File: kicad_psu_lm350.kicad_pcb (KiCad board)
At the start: 2 copper layers, 149.9 x 83.8 mm, 28 parts, among them J1 AC Input, J2 AC Input, J3 DC +1.25 to +30V, J4 GND, J5 GND, J6 GND, J7 GND, U1 LM350_TO220

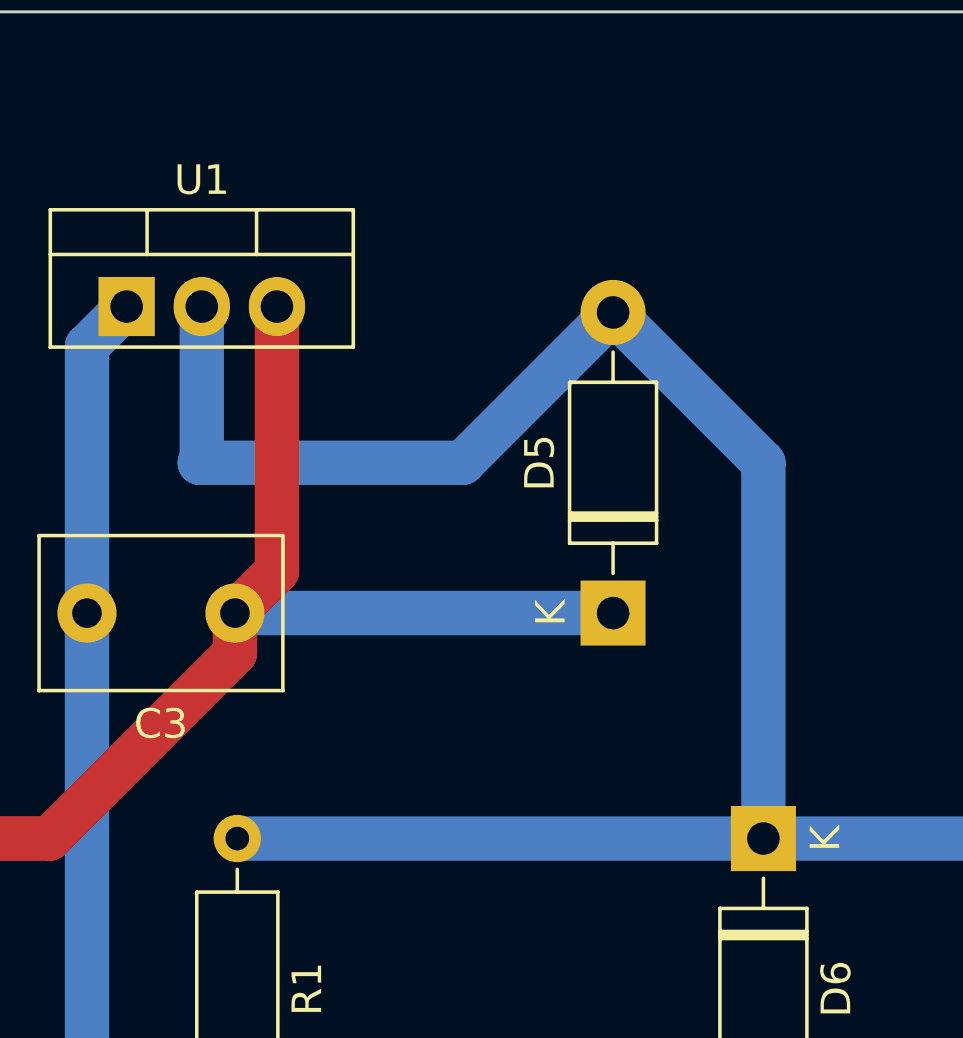
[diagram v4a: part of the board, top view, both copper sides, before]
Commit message: Created prototype - manufactured on pcbway.com
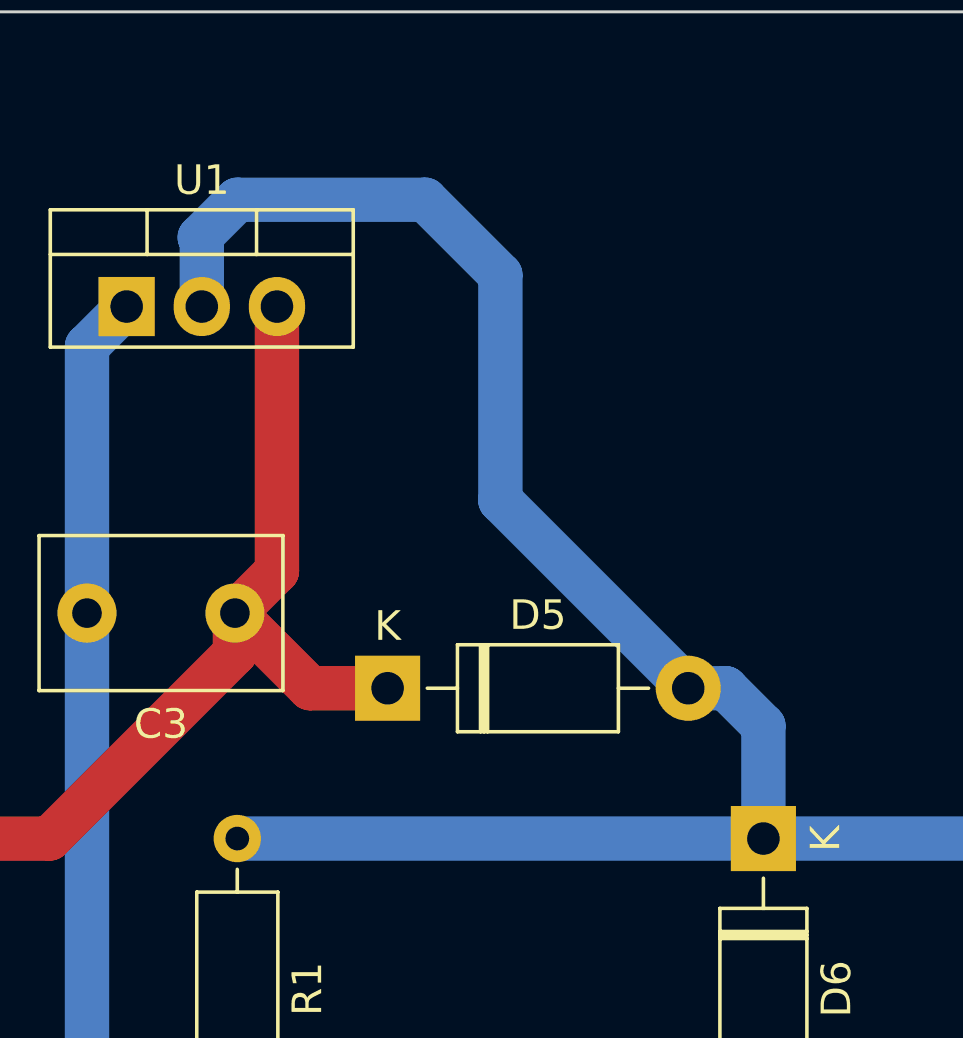
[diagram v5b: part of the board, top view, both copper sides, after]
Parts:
- moved D5 8.03 mm to (215.9, 50.8), turned to 0 degrees
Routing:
- net Net-(C1-Pad1): track 137.4 -> 130.8 mm
- net Net-(C5-Pad1): track 114.6 -> 110.9 mm
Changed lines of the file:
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@@
       (disableapertmacros false)
       (usegerberextensions false)
-      (usegerberattributes true)
-      (usegerberadvancedattributes true)
-      (creategerberjobfile true)
+      (usegerberattributes false)
+      (usegerberadvancedattributes false)
+      (creategerberjobfile false)
       (dashed_line_dash_ratio 12.000000)
       (dashed_line_gap_ratio 3.000000)
@@
       (psa4output false)
       (plotreference true)
-      (plotvalue true)
+      (plotvalue false)
       (plotinvisibletext false)
       (sketchpadsonfab false)
-      (subtractmaskfromsilk false)
+      (subtractmaskfromsilk true)
       (outputformat 1)
       (mirror false)
-      (drillshape 1)
+      (drillshape 0)
       (scaleselection 1)
-      (outputdirectory "")
+      (outputdirectory "outputs/pcbway/")
     )
   )
@@
   )
   (footprint "Diode_THT:D_DO-41_SOD81_P10.16mm_Horizontal" (layer "F.Cu")
-    (at 223.52 48.26 90)
+    (at 215.9 50.8)
     (descr "Diode, DO-41_SOD81 series, Axial, Horizontal, pin pitch=10.16mm, , length*diameter=5.2*2.7mm^2, , http://www.diodes.com/_files/packages/DO-41%20(Plastic).pdf")
     (tags "Diode DO-41_SOD81 series Axial Horizontal pin pitch 10.16mm  length 5.2mm diameter 2.7mm")
@@
     (property "Sheetname" "")
     (attr through_hole)
-    (fp_text reference "D5" (at 5.08 -2.47 90) (layer "F.SilkS")
+    (fp_text reference "D5" (at 5.08 -2.47) (layer "F.SilkS")
         (effects (font (size 1 1) (thickness 0.15)))
     )
-    (fp_text value "1N4007" (at 5.08 2.47 90) (layer "F.Fab")
+    (fp_text value "1N4007" (at 5.08 2.47) (layer "F.Fab")
         (effects (font (size 1 1) (thickness 0.15)))
     )
-    (fp_text user "K" (at 0 -2.1 90) (layer "F.SilkS")
+    (fp_text user "K" (at 0 -2.1) (layer "F.SilkS")
         (effects (font (size 1 1) (thickness 0.15)))
     )
-    (fp_text user "K" (at 0 -2.1 90) (layer "F.Fab")
+    (fp_text user "K" (at 0 -2.1) (layer "F.Fab")
         (effects (font (size 1 1) (thickness 0.15)))
     )
-    (fp_text user "${REFERENCE}" (at 5.47 0 90) (layer "F.Fab")
+    (fp_text user "${REFERENCE}" (at 5.47 0) (layer "F.Fab")
         (effects (font (size 1 1) (thickness 0.15)))
     )
@@
     (fp_line (start 10.16 0) (end 7.68 0)
       (stroke (width 0.1) (type solid)) (layer "F.Fab"))
-    (pad "1" thru_hole rect (at 0 0 90) (size 2.2 2.2) (drill 1.1) (layers "*.Cu" "*.Mask")
+    (pad "1" thru_hole rect (at 0 0) (size 2.2 2.2) (drill 1.1) (layers "*.Cu" "*.Mask")
       (net 4 "Net-(C1-Pad1)") (pinfunction "K") (pintype "passive"))
-    (pad "2" thru_hole oval (at 10.16 0 90) (size 2.2 2.2) (drill 1.1) (layers "*.Cu" "*.Mask")
+    (pad "2" thru_hole oval (at 10.16 0) (size 2.2 2.2) (drill 1.1) (layers "*.Cu" "*.Mask")
       (net 1 "Net-(C5-Pad1)") (pinfunction "A") (pintype "passive"))
     (model "${KICAD6_3DMODEL_DIR}/Diode_THT.3dshapes/D_DO-41_SOD81_P10.16mm_Horizontal.wrl"
@@
     (pts (xy 116.84 111.76) (xy 266.7 111.76))
     (height 5.08)
-    (gr_text "149.8600 mm" (at 191.77 115.69) (layer "Dwgs.User")
+    (gr_text "5.9000 in" (at 191.77 115.69) (layer "Dwgs.User")
       (effects (font (size 1 1) (thickness 0.15)))
     )
@@
     (pts (xy 116.84 27.94) (xy 116.84 111.76))
     (height 7.62)
-    (gr_text "83.8200 mm" (at 108.07 69.85 90) (layer "Dwgs.User")
+    (gr_text "3.3000 in" (at 108.07 69.85 90) (layer "Dwgs.User")
       (effects (font (size 1 1) (thickness 0.15)))
     )
@@
   (via (at 259.08 35.56) (size 5) (drill 3) (layers "F.Cu" "B.Cu") (net 0))
   (via (at 124.46 104.14) (size 5) (drill 3) (layers "F.Cu" "B.Cu") (net 0))
-  (segment (start 209.62 43.11) (end 209.62 37.9) (width 1.5) (layer "B.Cu") (net 1))
   (segment (start 242.26 82.86) (end 247.65 77.47) (width 1.5) (layer "B.Cu") (net 1))
+  (segment (start 219.71 44.45) (end 219.71 36.83) (width 1.5) (layer "B.Cu") (net 1))
+  (segment (start 210.82 34.29) (end 209.55 35.56) (width 1.5) (layer "B.Cu") (net 1))
   (segment (start 241.3 55.88) (end 247.65 55.88) (width 1.5) (layer "B.Cu") (net 1))
-  (segment (start 209.55 43.18) (end 209.62 43.11) (width 1.5) (layer "B.Cu") (net 1))
   (segment (start 242.26 83.82) (end 242.26 82.86) (width 1.5) (layer "B.Cu") (net 1))
+  (segment (start 217.17 34.29) (end 210.82 34.29) (width 1.5) (layer "B.Cu") (net 1))
   (segment (start 247.65 55.88) (end 254 55.88) (width 1.5) (layer "B.Cu") (net 1))
   (segment (start 228.6 55.88) (end 241.3 55.88) (width 1.5) (layer "B.Cu") (net 1))
-  (segment (start 223.52 38.1) (end 218.44 43.18) (width 1.5) (layer "B.Cu") (net 1))
-  (segment (start 228.6 55.88) (end 228.6 43.18) (width 1.5) (layer "B.Cu") (net 1))
+  (segment (start 226.06 50.8) (end 227.33 50.8) (width 1.5) (layer "B.Cu") (net 1))
+  (segment (start 219.71 36.83) (end 217.17 34.29) (width 1.5) (layer "B.Cu") (net 1))
+  (segment (start 227.33 50.8) (end 228.6 52.07) (width 1.5) (layer "B.Cu") (net 1))
   (segment (start 247.65 77.47) (end 247.65 55.88) (width 1.5) (layer "B.Cu") (net 1))
   (segment (start 210.82 55.88) (end 228.6 55.88) (width 1.5) (layer "B.Cu") (net 1))
-  (segment (start 218.44 43.18) (end 209.55 43.18) (width 1.5) (layer "B.Cu") (net 1))
-  (segment (start 228.6 43.18) (end 223.52 38.1) (width 1.5) (layer "B.Cu") (net 1))
+  (segment (start 209.55 35.56) (end 209.62 35.63) (width 1.5) (layer "B.Cu") (net 1))
+  (segment (start 226.06 50.8) (end 219.71 44.45) (width 1.5) (layer "B.Cu") (net 1))
+  (segment (start 228.6 52.07) (end 228.6 55.88) (width 1.5) (layer "B.Cu") (net 1))
+  (segment (start 209.62 35.63) (end 209.62 37.9) (width 1.5) (layer "B.Cu") (net 1))
   (segment (start 205.74 64.77) (end 207.01 66.04) (width 1.5) (layer "B.Cu") (net 2))
   (segment (start 222.25 69.85) (end 215.9 69.85) (width 1.5) (layer "B.Cu") (net 2))
@@
   (segment (start 172.72 81.2) (end 167.72 81.2) (width 1.5) (layer "B.Cu") (net 3))
   (segment (start 210.74 49.61) (end 204.47 55.88) (width 1.5) (layer "F.Cu") (net 4))
+  (segment (start 215.9 50.8) (end 213.28 50.8) (width 1.5) (layer "F.Cu") (net 4))
   (segment (start 210.74 48.26) (end 210.74 49.61) (width 1.5) (layer "F.Cu") (net 4))
   (segment (start 212.16 37.9) (end 212.16 46.84) (width 1.5) (layer "F.Cu") (net 4))
   (segment (start 212.16 46.84) (end 210.74 48.26) (width 1.5) (layer "F.Cu") (net 4))
+  (segment (start 213.28 50.8) (end 210.74 48.26) (width 1.5) (layer "F.Cu") (net 4))
   (segment (start 193.04 55.88) (end 187.96 60.96) (width 1.5) (layer "F.Cu") (net 4))
   (segment (start 204.47 55.88) (end 193.04 55.88) (width 1.5) (layer "F.Cu") (net 4))
@@
   (segment (start 144.78 45.72) (end 152.4 38.1) (width 1.5) (layer "B.Cu") (net 4))
   (segment (start 177.8 50.8) (end 187.96 60.96) (width 1.5) (layer "B.Cu") (net 4))
-  (segment (start 223.52 48.26) (end 210.74 48.26) (width 1.5) (layer "B.Cu") (net 4))
   (segment (start 190.5 86.36) (end 187.96 83.82) (width 1.5) (layer "B.Cu") (net 4))
   (segment (start 172.72 50.8) (end 177.8 50.8) (width 1.5) (layer "B.Cu") (net 4))
